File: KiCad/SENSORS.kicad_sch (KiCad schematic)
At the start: 8 parts, among them U5 TMP102xxDRL, U6 A1104xLH

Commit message: Canvis al KICAD
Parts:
- renumbered C9 to C1, D3 to D1, R12 to R1, R10 to R2, R11 to R3, R13 to R4, U5 to U1, U6 to U2
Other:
- moved on the sheet: C1, D1, R1, R2, R3, R4, U1, U2

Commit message: Afegist el MOSFET
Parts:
- renumbered C1 to C9, D1 to D3, R2 to R10, R3 to R11, R1 to R12, R4 to R13, U1 to U5, U2 to U6
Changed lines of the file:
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@@
 		(on_board yes)
 		(dnp no)
-		(property "Reference" "R3"
+		(property "Reference" "R11"
 			(at 81.28 90.17 0)
 			(effects
@@
 		(dnp no)
 		(fields_autoplaced yes)
-		(property "Reference" "C1"
+		(property "Reference" "C9"
 			(at 118.11 93.9799 0)
 			(effects
@@
 		(on_board yes)
 		(dnp no)
-		(property "Reference" "U1"
+		(property "Reference" "U5"
 			(at 91.948 72.136 0)
 			(effects
@@
 		(dnp no)
 		(fields_autoplaced yes)
-		(property "Reference" "D1"
+		(property "Reference" "D3"
 			(at 195.58 75.2474 90)
 			(effects
@@
 		(dnp no)
 		(fields_autoplaced yes)
-		(property "Reference" "R1"
+		(property "Reference" "R12"
 			(at 194.31 85.0899 0)
 			(effects
@@
 		(dnp no)
 		(fields_autoplaced yes)
-		(property "Reference" "U2"
+		(property "Reference" "U6"
 			(at 172.72 95.2499 0)
 			(effects
@@
 		(dnp no)
 		(fields_autoplaced yes)
-		(property "Reference" "R4"
+		(property "Reference" "R13"
 			(at 123.19 74.93 90)
 			(effects
@@
 		(dnp no)
 		(fields_autoplaced yes)
-		(property "Reference" "R2"
+		(property "Reference" "R10"
 			(at 80.01 72.3899 0)
 			(effects

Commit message: Modificacio
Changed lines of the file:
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@@
+	(wire
+		(pts
+			(xy 66.04 83.82) (xy 66.04 86.36)
+		)
+		(stroke
+			(width 0)
+			(type default)
+		)
+	)
 	(wire
 		(pts
@@
 		(pts
 			(xy 114.3 101.6) (xy 100.33 101.6)
+		)
+		(stroke
+			(width 0)
+			(type default)
+		)
+	)
+	(wire
+		(pts
+			(xy 66.04 78.74) (xy 66.04 81.28)
 		)
 		(stroke
@@
 	(global_label "I2C_SDA"
 		(shape bidirectional)
-		(at 66.04 81.28 180)
-		(fields_autoplaced yes)
-		(effects
-			(font
-				(size 1.27 1.27)
-			)
-			(justify right)
-		)
-		(property "Intersheetrefs" "${INTERSHEET_REFS}"
-			(at 54.3235 81.28 0)
+		(at 66.04 78.74 180)
+		(fields_autoplaced yes)
+		(effects
+			(font
+				(size 1.27 1.27)
+			)
+			(justify right)
+		)
+		(property "Intersheetrefs" "${INTERSHEET_REFS}"
+			(at 54.3235 78.74 0)
 			(effects
 				(font
@@
 	(global_label "I2C_SCL"
 		(shape bidirectional)
-		(at 66.04 83.82 180)
-		(fields_autoplaced yes)
-		(effects
-			(font
-				(size 1.27 1.27)
-			)
-			(justify right)
-		)
-		(property "Intersheetrefs" "${INTERSHEET_REFS}"
-			(at 54.384 83.82 0)
-			(effects
-				(font
+		(at 66.04 86.36 180)
+		(fields_autoplaced yes)
+		(effects
+			(font
+				(size 1.27 1.27)
+			)
+			(justify right)
+		)
+		(property "Intersheetrefs" "${INTERSHEET_REFS}"
+			(at 54.384 86.36 0)
+			(effects
+				(font

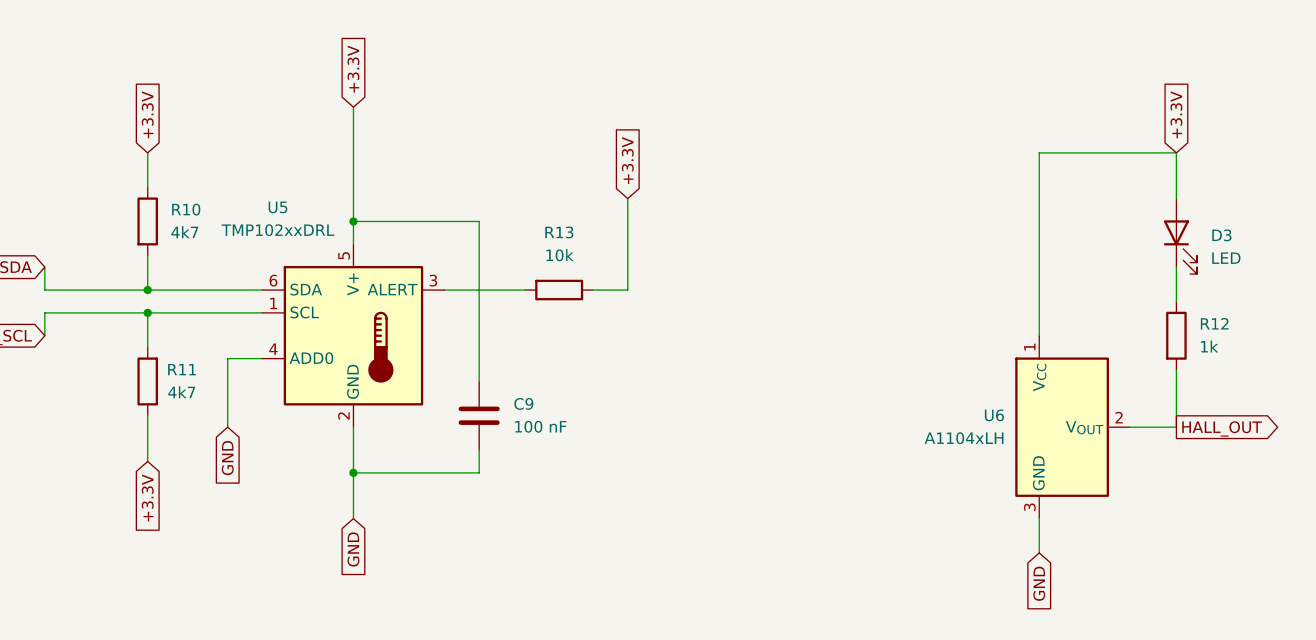
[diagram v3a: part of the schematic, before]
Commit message: Afegist el MOSFET
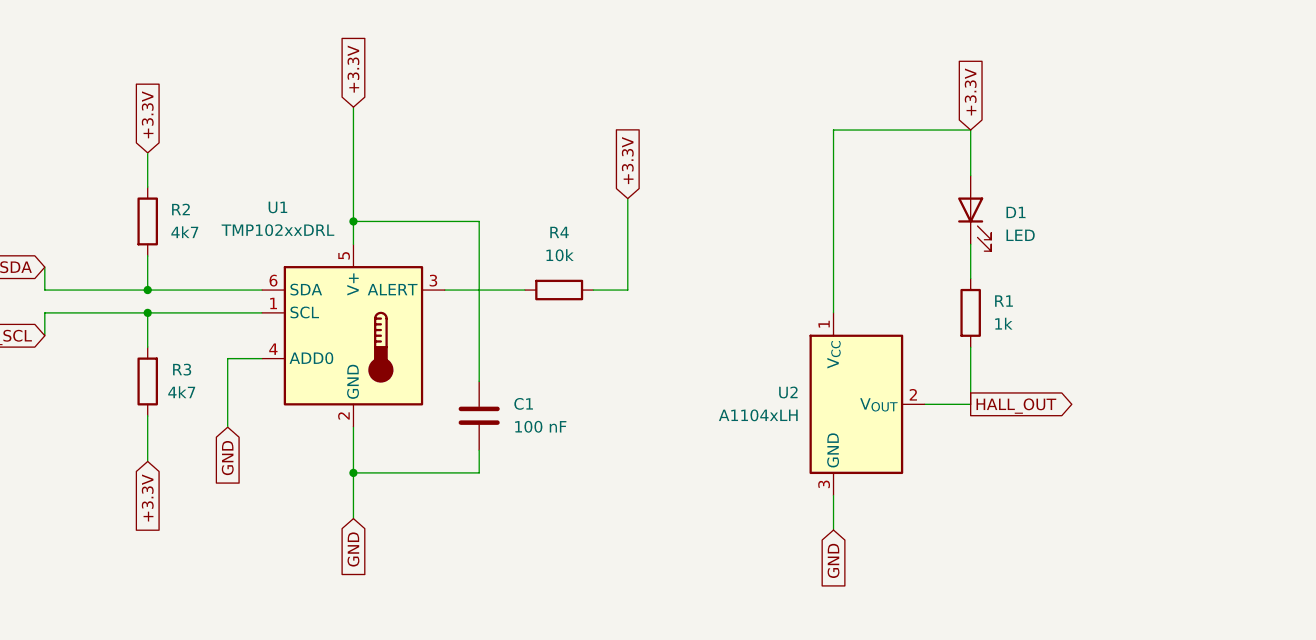
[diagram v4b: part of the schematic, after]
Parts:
- renumbered C9 to C1, D3 to D1, R12 to R1, R10 to R2, R11 to R3, R13 to R4, U5 to U1, U6 to U2
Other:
- moved on the sheet: D1, R1, U2
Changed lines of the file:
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@@
 	(wire
 		(pts
-			(xy 186.69 96.52) (xy 191.77 96.52)
+			(xy 163.83 93.98) (xy 168.91 93.98)
 		)
 		(stroke
@@
 	(wire
 		(pts
-			(xy 176.53 66.04) (xy 191.77 66.04)
+			(xy 153.67 63.5) (xy 168.91 63.5)
 		)
 		(stroke
@@
 	(wire
 		(pts
-			(xy 191.77 78.74) (xy 191.77 82.55)
+			(xy 168.91 76.2) (xy 168.91 80.01)
 		)
 		(stroke
@@
 	(wire
 		(pts
-			(xy 176.53 106.68) (xy 176.53 110.49)
+			(xy 153.67 104.14) (xy 153.67 107.95)
 		)
 		(stroke
@@
 	(wire
 		(pts
-			(xy 176.53 86.36) (xy 176.53 66.04)
+			(xy 153.67 83.82) (xy 153.67 63.5)
 		)
 		(stroke
@@
 	(wire
 		(pts
-			(xy 191.77 96.52) (xy 191.77 90.17)
+			(xy 168.91 93.98) (xy 168.91 87.63)
 		)
 		(stroke
@@
 	(wire
 		(pts
-			(xy 191.77 66.04) (xy 191.77 71.12)
+			(xy 168.91 63.5) (xy 168.91 68.58)
 		)
 		(stroke
@@
 	(global_label "GND"
 		(shape input)
-		(at 176.53 110.49 270)
+		(at 153.67 107.95 270)
 		(fields_autoplaced yes)
 		(effects
@@
 		)
 		(property "Intersheetrefs" "${INTERSHEET_REFS}"
-			(at 176.53 116.6915 90)
+			(at 153.67 114.1515 90)
 			(effects
 				(font
@@
 	(global_label "+3.3V"
 		(shape input)
-		(at 191.77 66.04 90)
+		(at 168.91 63.5 90)
 		(fields_autoplaced yes)
 		(effects
@@
 		)
 		(property "Intersheetrefs" "${INTERSHEET_REFS}"
-			(at 191.77 57.37 90)
+			(at 168.91 54.83 90)
 			(effects
 				(font
@@
 	(global_label "HALL_OUT"
 		(shape output)
-		(at 191.77 96.52 0)
+		(at 168.91 93.98 0)
 		(fields_autoplaced yes)
 		(effects
@@
 		)
 		(property "Intersheetrefs" "${INTERSHEET_REFS}"
-			(at 203.8267 96.52 0)
+			(at 180.9667 93.98 0)
 			(effects
 				(font
@@
 		(on_board yes)
 		(dnp no)
-		(property "Reference" "R11"
+		(property "Reference" "R3"
 			(at 81.28 90.17 0)
 			(effects
@@
 		(dnp no)
 		(fields_autoplaced yes)
-		(property "Reference" "C9"
+		(property "Reference" "C1"
 			(at 118.11 93.9799 0)
 			(effects
@@
 		(on_board yes)
 		(dnp no)
-		(property "Reference" "U5"
+		(property "Reference" "U1"
 			(at 91.948 72.136 0)
 			(effects
@@
 	(symbol
 		(lib_id "Device:LED")
-		(at 191.77 74.93 90)
+		(at 168.91 72.39 90)
 		(unit 1)
 		(exclude_from_sim no)
@@
 		(dnp no)
 		(fields_autoplaced yes)
-		(property "Reference" "D3"
-			(at 195.58 75.2474 90)
+		(property "Reference" "D1"
+			(at 172.72 72.7074 90)
 			(effects
 				(font
@@
 		)
 		(property "Value" "LED"
-			(at 195.58 77.7874 90)
+			(at 172.72 75.2474 90)
 			(effects
 				(font
@@
 		)
 		(property "Footprint" ""
-			(at 191.77 74.93 0)
+			(at 168.91 72.39 0)
 			(effects
 				(font
@@
 		)
 		(property "Datasheet" "~"
-			(at 191.77 74.93 0)
+			(at 168.91 72.39 0)
 			(effects
 				(font
@@
 		)
 		(property "Description" "Light emitting diode"
-			(at 191.77 74.93 0)
+			(at 168.91 72.39 0)
 			(effects
 				(font
@@
 		)
 		(property "Sim.Pins" "1=K 2=A"
-			(at 191.77 74.93 0)
+			(at 168.91 72.39 0)
 			(effects
 				(font
@@
 	(symbol
 		(lib_id "Device:R")
-		(at 191.77 86.36 0)
+		(at 168.91 83.82 0)
 		(unit 1)
 		(exclude_from_sim no)
@@
 		(dnp no)
 		(fields_autoplaced yes)
-		(property "Reference" "R12"
-			(at 194.31 85.0899 0)
+		(property "Reference" "R1"
+			(at 171.45 82.5499 0)
 			(effects
 				(font
@@
 		)
 		(property "Value" "1k"
-			(at 194.31 87.6299 0)
+			(at 171.45 85.0899 0)
 			(effects
 				(font
@@
 		)
 		(property "Footprint" ""
-			(at 189.992 86.36 90)
+			(at 167.132 83.82 90)
 			(effects
 				(font
@@
 		)
 		(property "Datasheet" "~"
-			(at 191.77 86.36 0)
+			(at 168.91 83.82 0)
 			(effects
 				(font
@@
 		)
 		(property "Description" "Resistor"
-			(at 191.77 86.36 0)
+			(at 168.91 83.82 0)
 			(effects
 				(font
@@
 	(symbol
 		(lib_id "Sensor_Magnetic:A1104xLH")
-		(at 179.07 96.52 0)
+		(at 156.21 93.98 0)
 		(unit 1)
 		(exclude_from_sim no)
@@
 		(dnp no)
 		(fields_autoplaced yes)
-		(property "Reference" "U6"
-			(at 172.72 95.2499 0)
+		(property "Reference" "U2"
+			(at 149.86 92.7099 0)
 			(effects
 				(font
@@
 		)
 		(property "Value" "A1104xLH"
-			(at 172.72 97.7899 0)
+			(at 149.86 95.2499 0)
 			(effects
 				(font
@@
 		)
 		(property "Footprint" "Package_TO_SOT_SMD:SOT-23W"
-			(at 179.07 113.792 0)
+			(at 156.21 111.252 0)
 			(effects
 				(font
@@
 		)
 		(property "Datasheet" "https://www.allegromicro.com/-/media/files/datasheets/a110x-datasheet.ashx"
-			(at 179.07 109.22 0)
+			(at 156.21 106.68 0)
 			(effects
 				(font
@@
 		)
 		(property "Description" "Hall effect switch, unipolar (south-polarity), Bop=70-350G, Brp=50-330G, 3.8-24V supply, SOT-23W"
-			(at 179.07 111.506 0)
+			(at 156.21 108.966 0)
 			(effects
 				(font
@@
 		(dnp no)
 		(fields_autoplaced yes)
-		(property "Reference" "R13"
+		(property "Reference" "R4"
 			(at 123.19 74.93 90)
 			(effects
@@
 		(dnp no)
 		(fields_autoplaced yes)
-		(property "Reference" "R10"
+		(property "Reference" "R2"
 			(at 80.01 72.3899 0)
 			(effects

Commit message: Millora
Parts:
- renumbered C1 to C9, D1 to D3, R2 to R10, R3 to R11, R1 to R12, R4 to R13, U1 to U5, U2 to U6
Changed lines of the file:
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@@
 		(on_board yes)
 		(dnp no)
-		(property "Reference" "R3"
+		(property "Reference" "R11"
 			(at 81.28 90.17 0)
 			(effects
@@
 		(dnp no)
 		(fields_autoplaced yes)
-		(property "Reference" "C1"
+		(property "Reference" "C9"
 			(at 118.11 93.9799 0)
 			(effects
@@
 		(on_board yes)
 		(dnp no)
-		(property "Reference" "U1"
+		(property "Reference" "U5"
 			(at 91.948 72.136 0)
 			(effects
@@
 		(dnp no)
 		(fields_autoplaced yes)
-		(property "Reference" "D1"
+		(property "Reference" "D3"
 			(at 172.72 72.7074 90)
 			(effects
@@
 		(dnp no)
 		(fields_autoplaced yes)
-		(property "Reference" "R1"
+		(property "Reference" "R12"
 			(at 171.45 82.5499 0)
 			(effects
@@
 		(dnp no)
 		(fields_autoplaced yes)
-		(property "Reference" "U2"
+		(property "Reference" "U6"
 			(at 149.86 92.7099 0)
 			(effects
@@
 		(dnp no)
 		(fields_autoplaced yes)
-		(property "Reference" "R4"
+		(property "Reference" "R13"
 			(at 123.19 74.93 90)
 			(effects
@@
 		(dnp no)
 		(fields_autoplaced yes)
-		(property "Reference" "R2"
+		(property "Reference" "R10"
 			(at 80.01 72.3899 0)
 			(effects

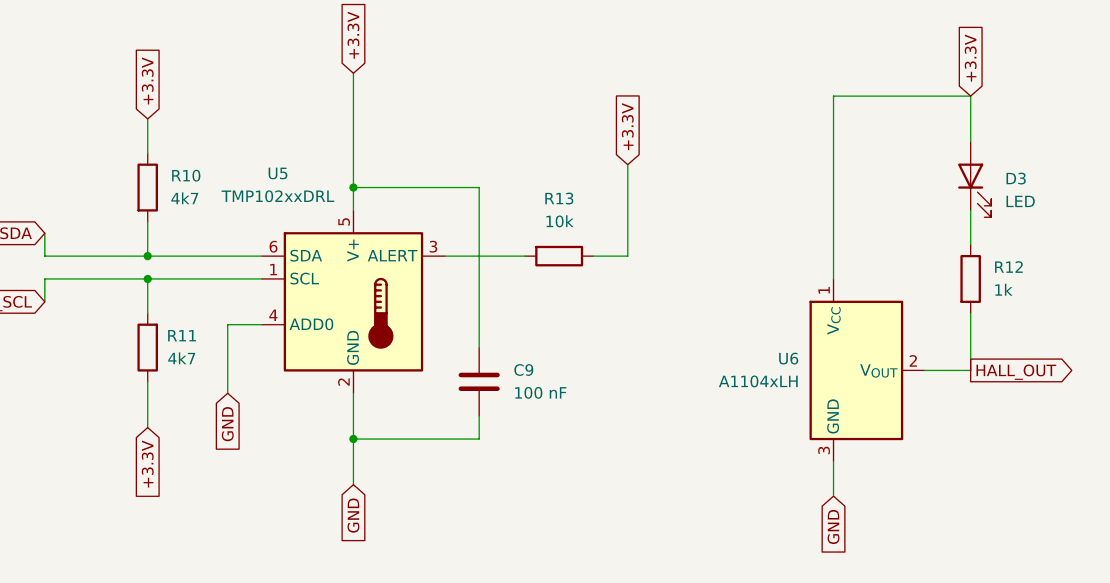
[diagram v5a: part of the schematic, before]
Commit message: cambios mejora ERC
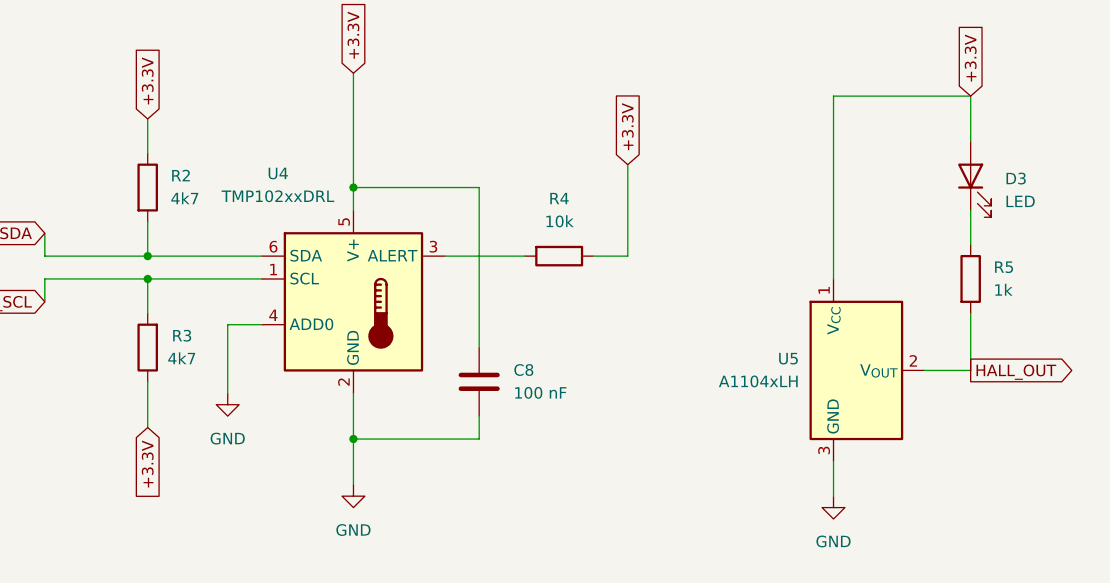
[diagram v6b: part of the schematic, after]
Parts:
- renumbered C9 to C8, R10 to R2, R11 to R3, R13 to R4, R12 to R5, U5 to U4, U6 to U5

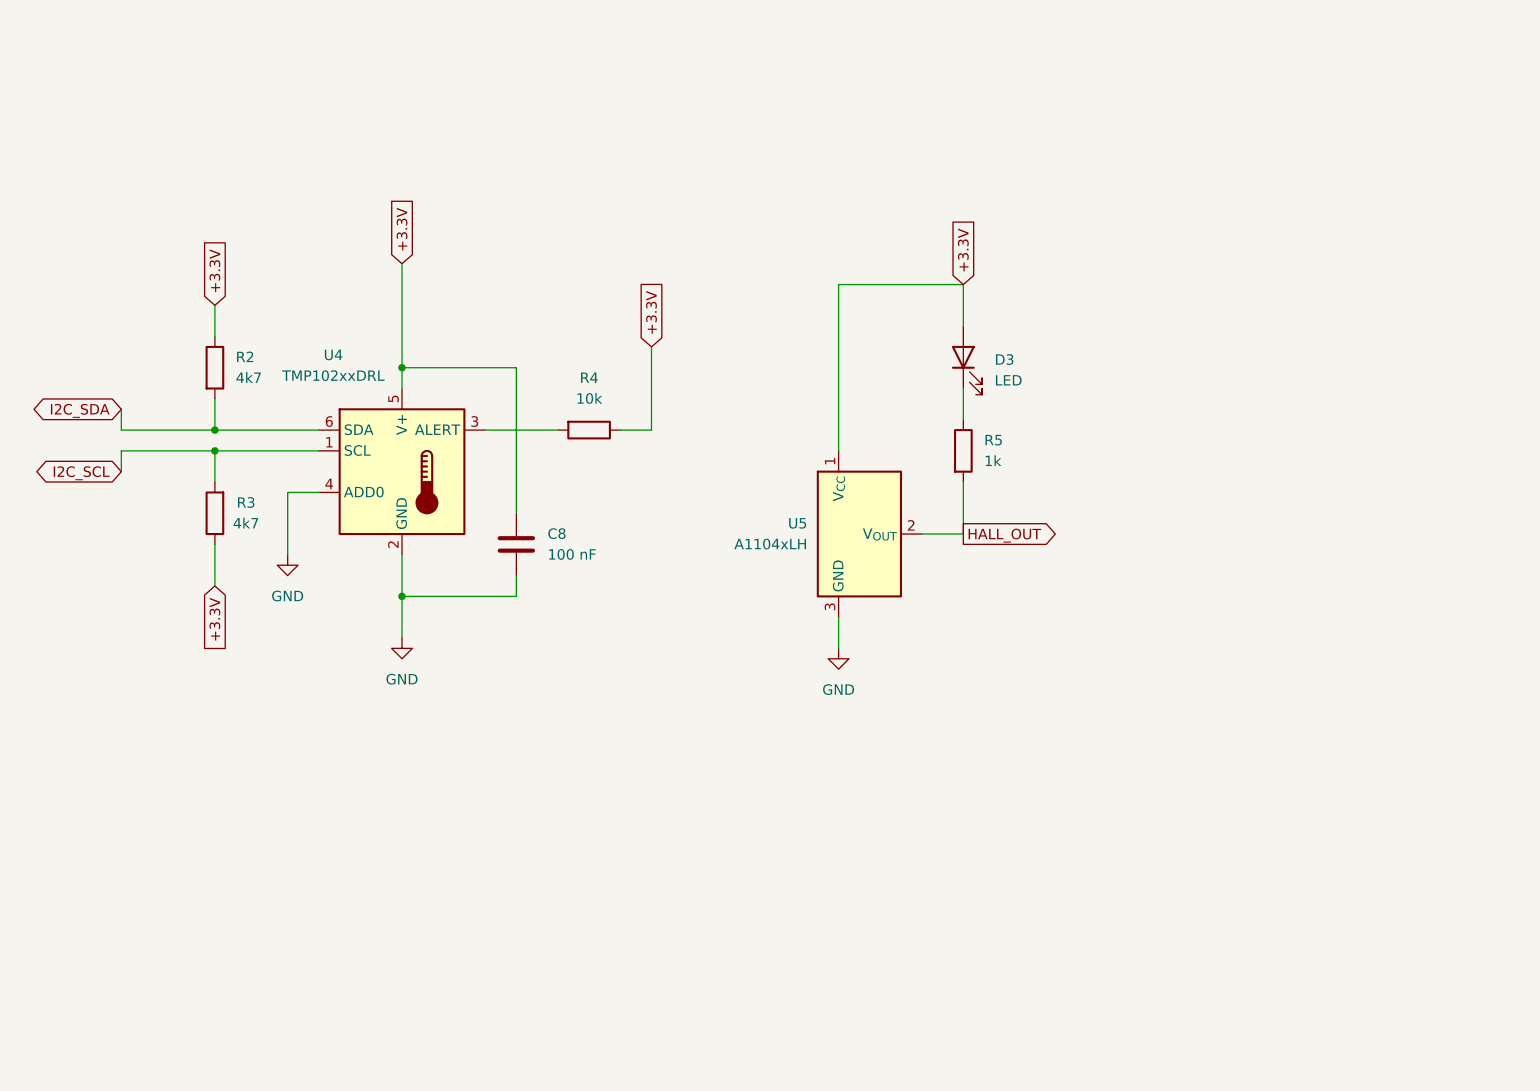
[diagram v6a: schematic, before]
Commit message: Modificacions al MICROCONTROLADOR
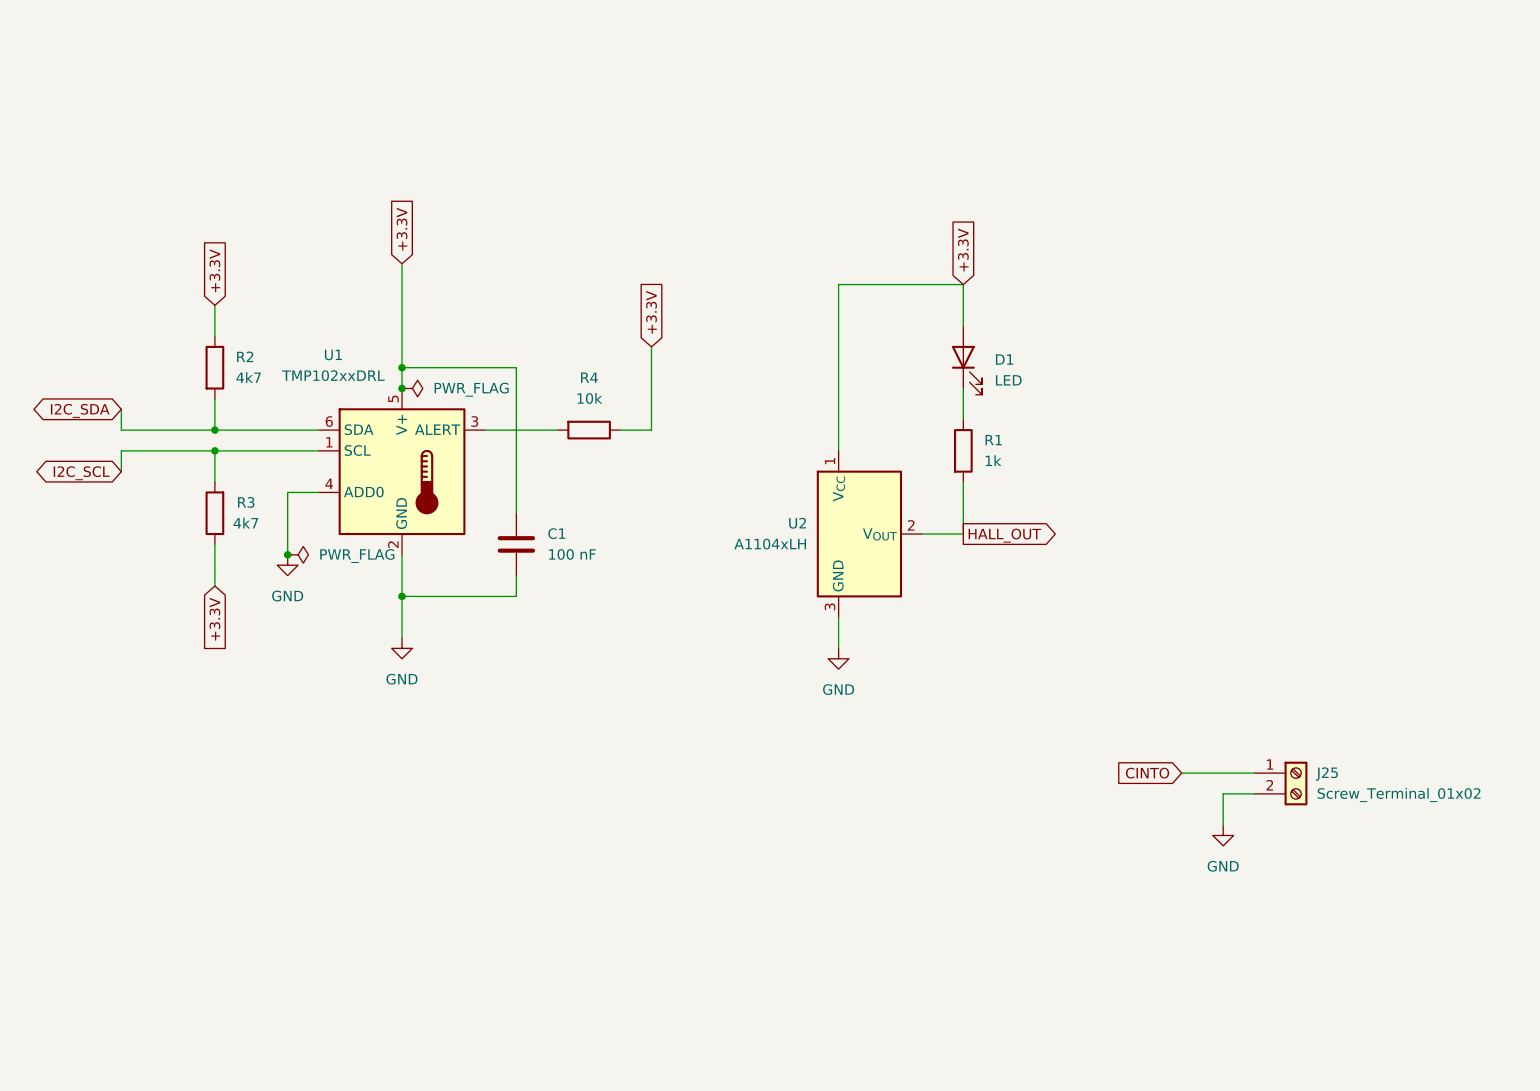
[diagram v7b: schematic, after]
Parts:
- added J25: Screw_Terminal_01x02, symbol Connector:Screw_Terminal_01x02
- renumbered C8 to C1, D3 to D1, R5 to R1, U4 to U1, U5 to U2
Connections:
- net GND: now also J25.2 (Pin_2)
- new net CINTO: J25.1 (Pin_1)
